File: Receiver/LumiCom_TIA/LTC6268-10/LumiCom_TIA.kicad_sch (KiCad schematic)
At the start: 0 parts

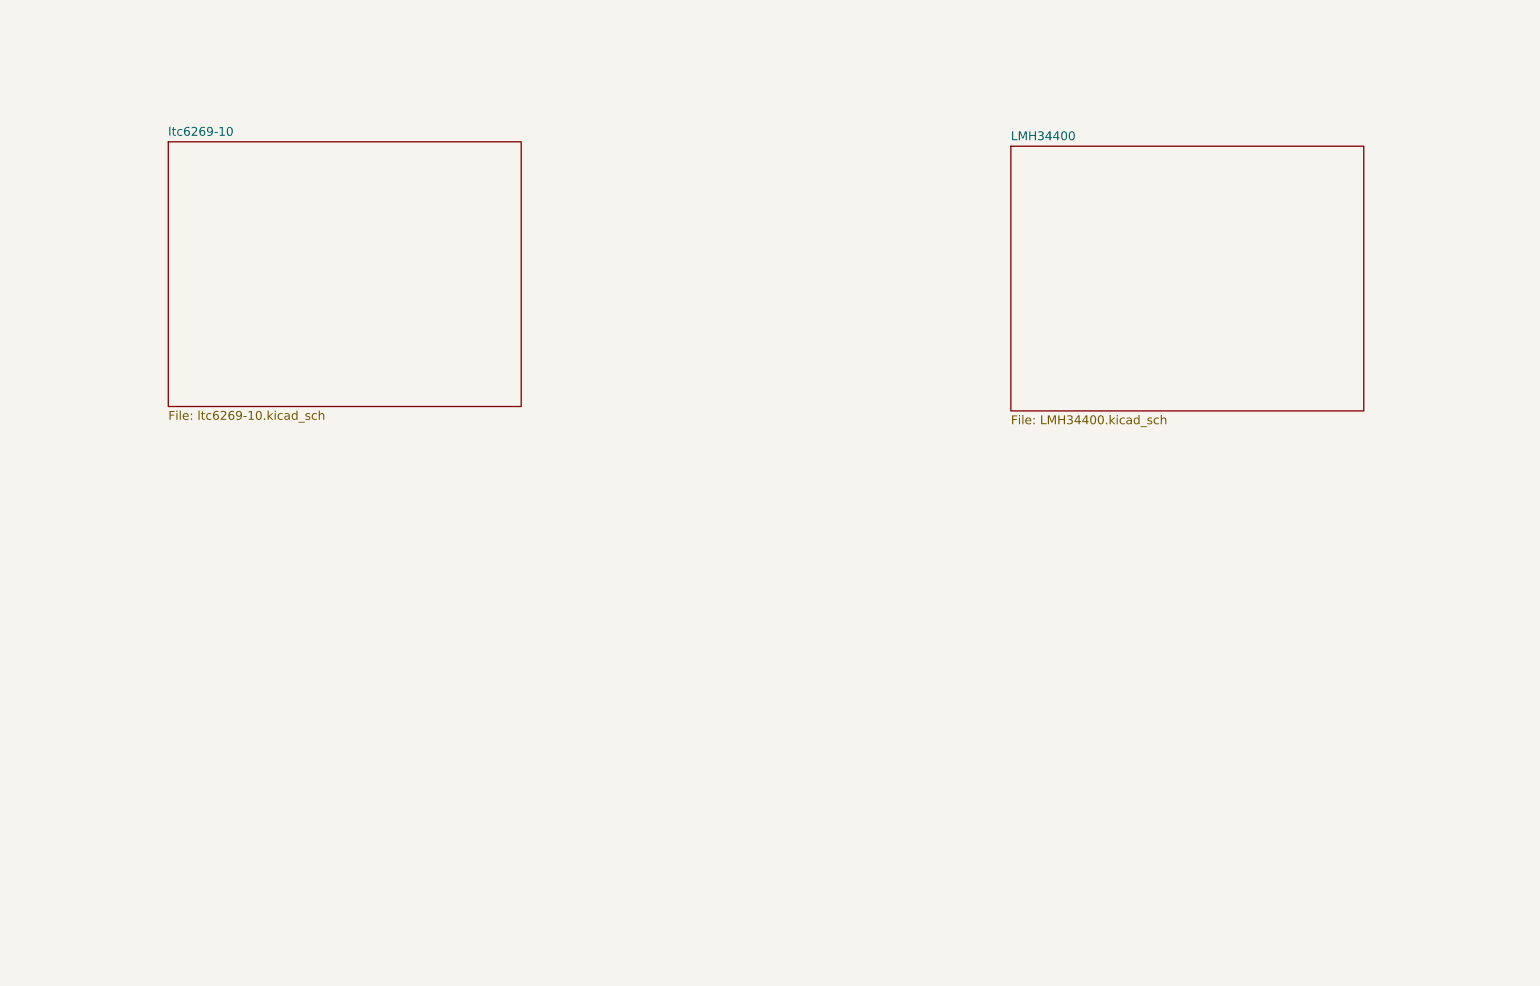
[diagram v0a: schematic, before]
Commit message: Multiple updates
SMA, Screw terminals, track widths, added some optional 0 ohm bypass resistors
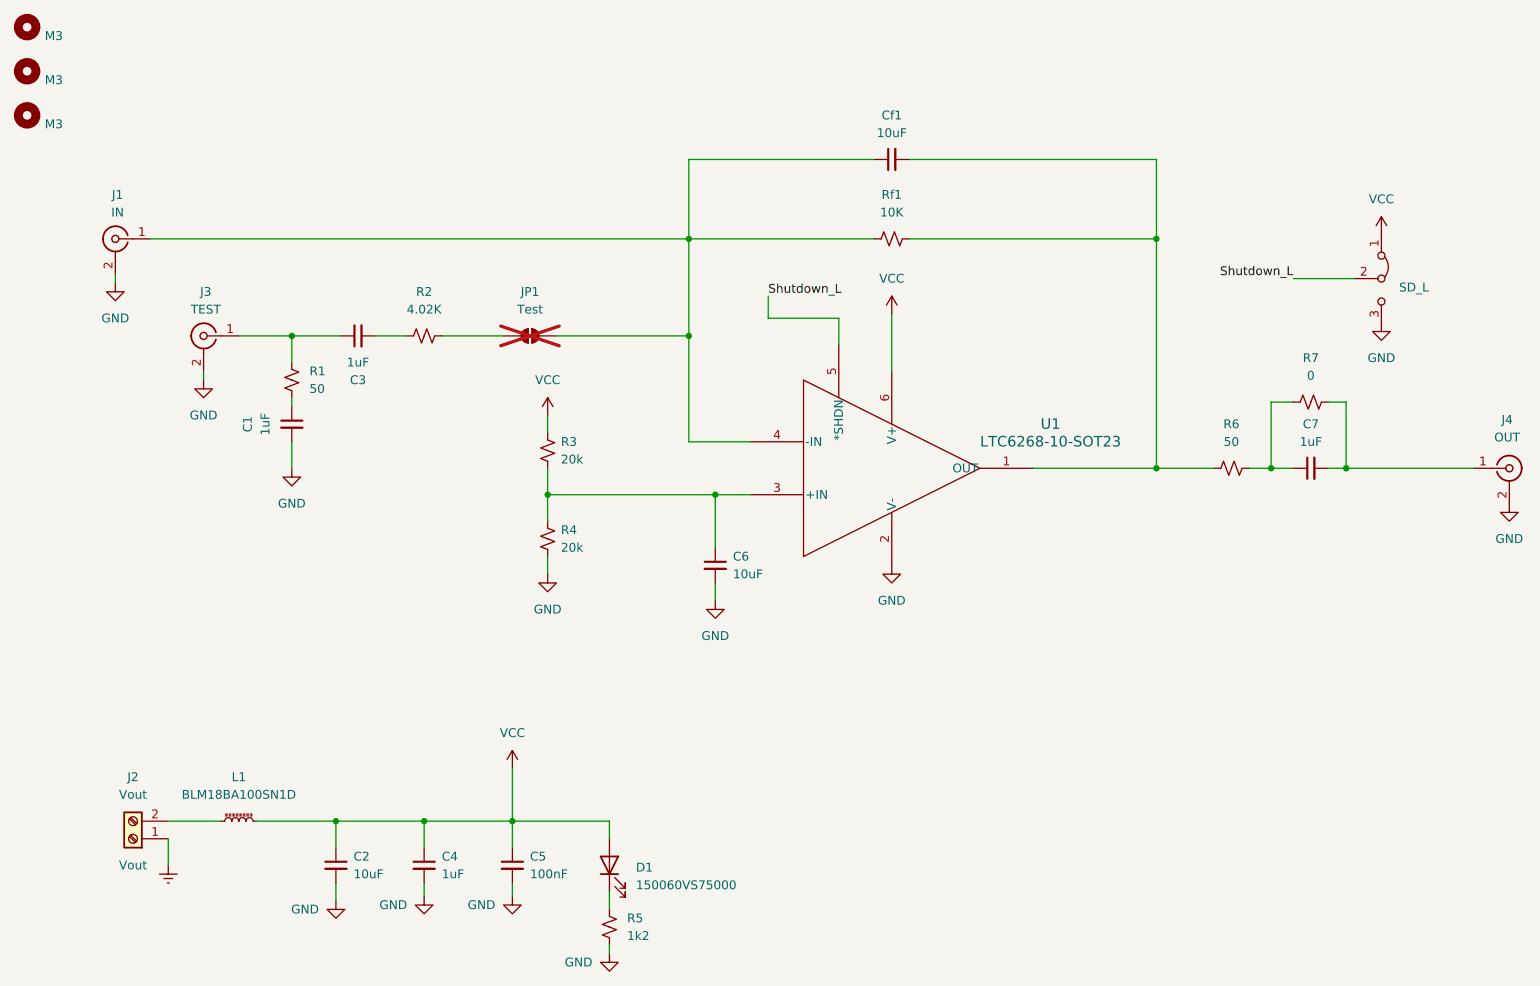
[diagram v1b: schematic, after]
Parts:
- added C1, C3, C4, C7: 1uF, Capacitor_SMD:C_0603_1608Metric_Pad1.08x0.95mm_HandSolder, symbol Device:C_Small
- added C2, C6, Cf1: 10uF, Capacitor_SMD:C_0603_1608Metric_Pad1.08x0.95mm_HandSolder, symbol Device:C_Small
- added C5: 100nF, Capacitor_SMD:C_0603_1608Metric_Pad1.08x0.95mm_HandSolder, symbol Device:C_Small
- added D1: 150060VS75000, LumiCom_TIA:LEDC1608X80N, symbol Device:LED
- added H1, H2, H3: M3, MountingHole:MountingHole_3.2mm_M3_DIN965, symbol Mechanical:MountingHole
- added J1: IN, Connector_Coaxial:SMA_Samtec_SMA-J-P-X-ST-EM1_EdgeMount, symbol Connector:Conn_Coaxial
- added J2: Vout, TerminalBlock_Phoenix:TerminalBlock_Phoenix_MKDS-1,5-2_1x02_P5.00mm_Horizontal, symbol Connector:Screw_Terminal_01x02
- added J3: TEST, Connector_Coaxial:SMA_Samtec_SMA-J-P-X-ST-EM1_EdgeMount, symbol Connector:Conn_Coaxial
- added J4: OUT, Connector_Coaxial:SMA_Samtec_SMA-J-P-X-ST-EM1_EdgeMount, symbol Connector:Conn_Coaxial
- added JP1: Test, Resistor_SMD:R_0603_1608Metric_Pad0.98x0.95mm_HandSolder, symbol Jumper:SolderJumper_2_Open
- added L1: BLM18BA100SN1D, Inductor_SMD:L_0603_1608Metric_Pad1.05x0.95mm_HandSolder, symbol Device:L_Ferrite_Small
- added R1, R6: 50, Resistor_SMD:R_0603_1608Metric_Pad0.98x0.95mm_HandSolder, symbol Device:R_Small_US
- added R2: 4.02K, Resistor_SMD:R_0603_1608Metric_Pad0.98x0.95mm_HandSolder, symbol Device:R_Small_US
- added R3, R4: 20k, Resistor_SMD:R_0603_1608Metric_Pad0.98x0.95mm_HandSolder, symbol Device:R_Small_US
- added R5: 1k2, Resistor_SMD:R_0603_1608Metric_Pad0.98x0.95mm_HandSolder, symbol Device:R_Small_US
- added R7: 0, Resistor_SMD:R_0603_1608Metric_Pad0.98x0.95mm_HandSolder, symbol Device:R_Small_US
- added Rf1: 10K, Resistor_SMD:R_0603_1608Metric_Pad0.98x0.95mm_HandSolder, symbol Device:R_Small_US
- added SD_L1: SD_L, Connector_PinHeader_2.54mm:PinHeader_1x03_P2.54mm_Vertical, symbol Jumper:Jumper_3_Bridged12
- added U1: LTC6268-10-SOT23, LumiCom_TIA:TSOT-23_S6_LIT, symbol LumiCom_TIA:LTC6268-10-SOT23
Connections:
- new net: C3.1, J3.1 (In), R1.1
- new net: C6.1, R3.2, R4.1, U1.3 (+IN)
- new net: J2.2 (Pin_2), L1.1
- new net: C3.2, R2.1
- new net: D1.1 (K), R5.1
- new net: Cf1.1, J1.1 (In), JP1.2 (B), Rf1.1, U1.4 (-IN)
- new net: Cf1.2, R6.1, Rf1.2, U1.1 (OUT)
- new net: C7.1, R6.2, R7.1
- new net: C7.2, J4.1 (In), R7.2
- new net: JP1.1 (A), R2.2
- new net: C1.1, R1.2
- new net GND: C1.2, C2.2, C4.2, C5.2, C6.2, J1.2 (Ext), J2.1 (Pin_1), J3.2 (Ext), J4.2 (Ext), R4.2, R5.2, SD_L1.3 (B), U1.2 (V-)
- new net Shutdown_L: SD_L1.2 (C), U1.5 (*SHDN)
- new net VCC: C2.1, C4.1, C5.1, D1.2 (A), L1.2, R3.1, SD_L1.1 (A), U1.6 (V+)
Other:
- removed sheet LMH34400
- removed sheet ltc6269-10
